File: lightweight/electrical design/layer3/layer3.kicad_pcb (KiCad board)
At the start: 2 copper layers, 188.9 x 115 mm, 59 parts, among them J1 SH1.0 5P, J11 SH1.0 5P, J2 SH1.0 5P, J3 SH1.0 5P, J4 SH1.0 5P, J5 Conn_01x03_Pin, J6 SH1.0 Female, SW1 SW_SPDT, SW2 SW_DPDT_x2, SW5 SW_Push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

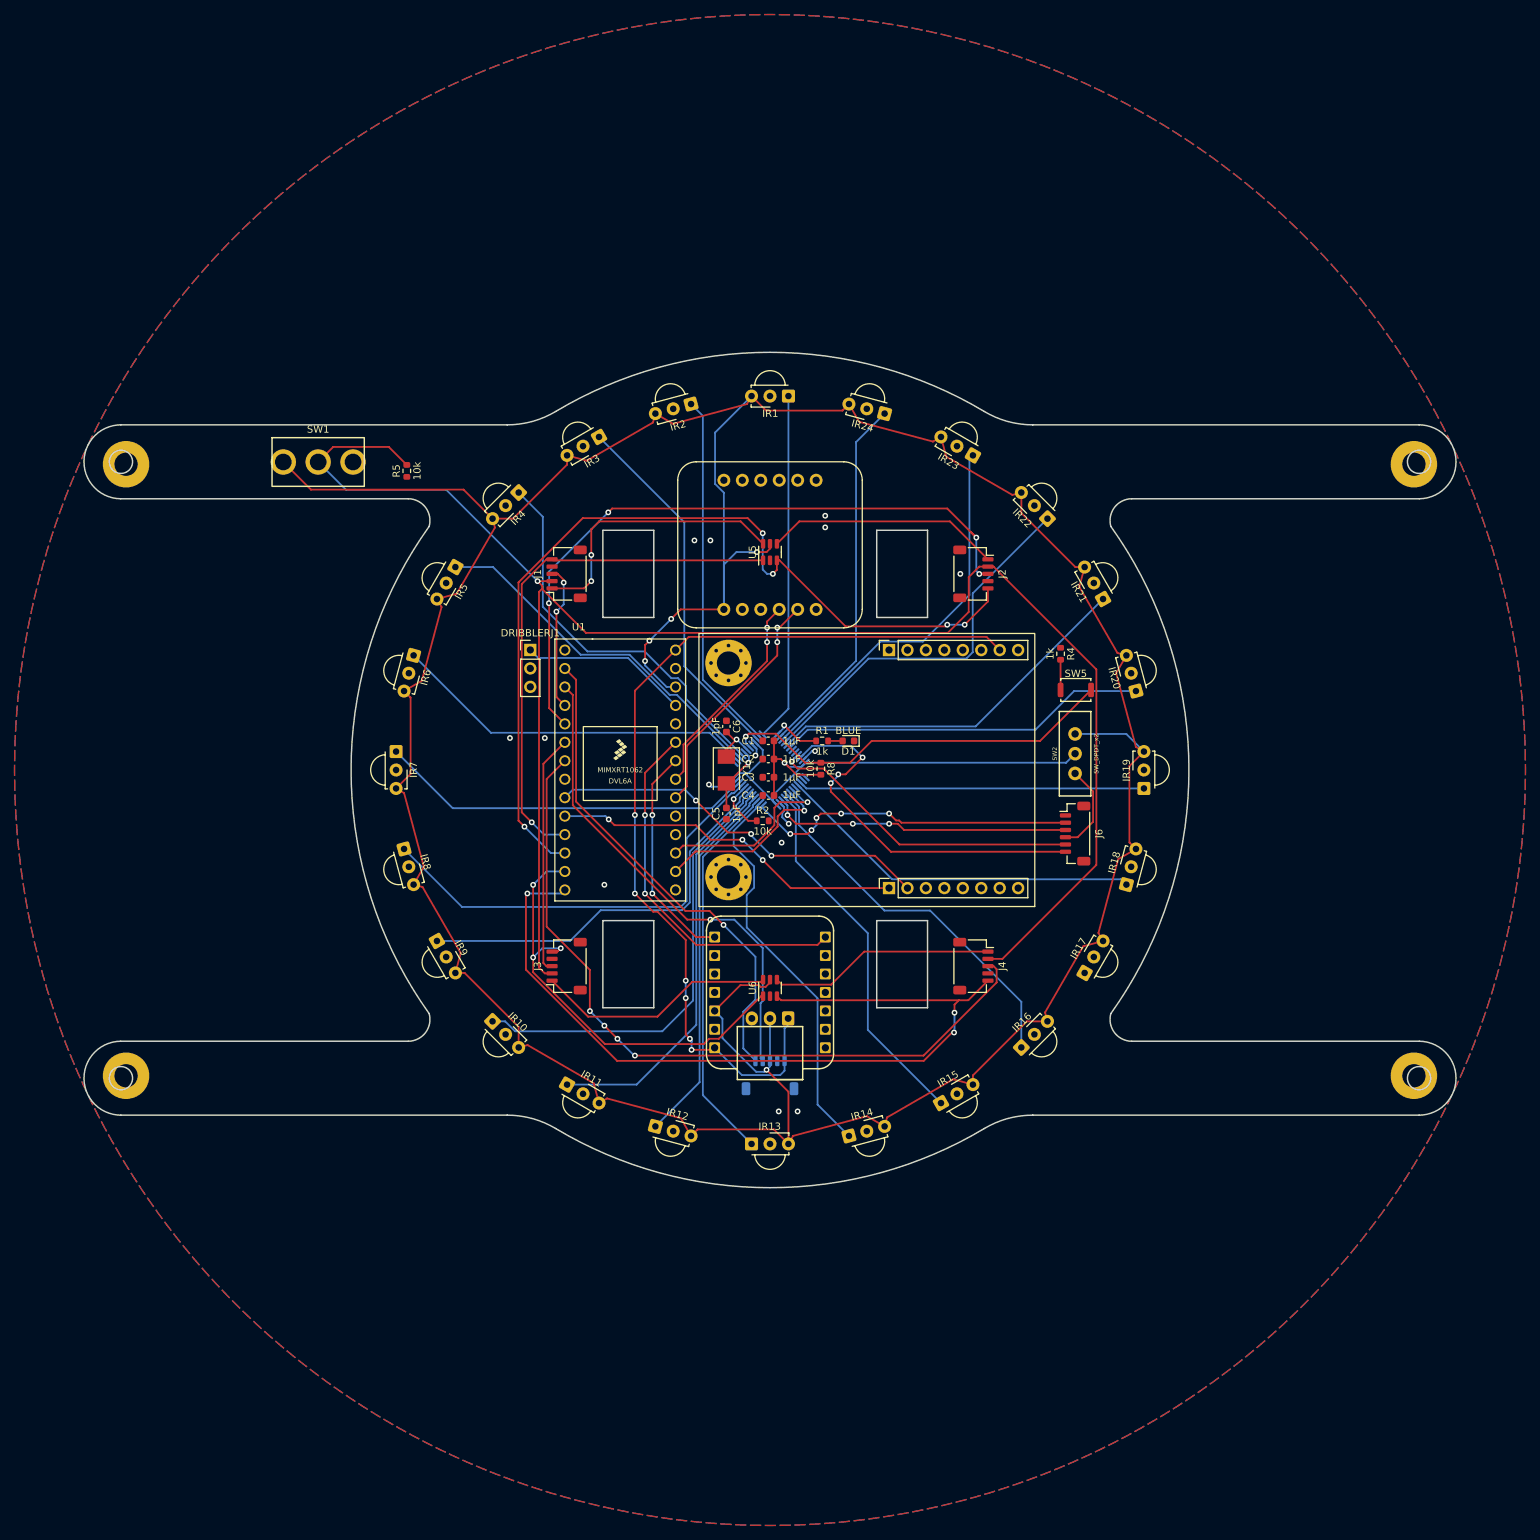
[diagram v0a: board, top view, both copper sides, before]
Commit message: fix drc faults on l1, l2, and l3 pcbs
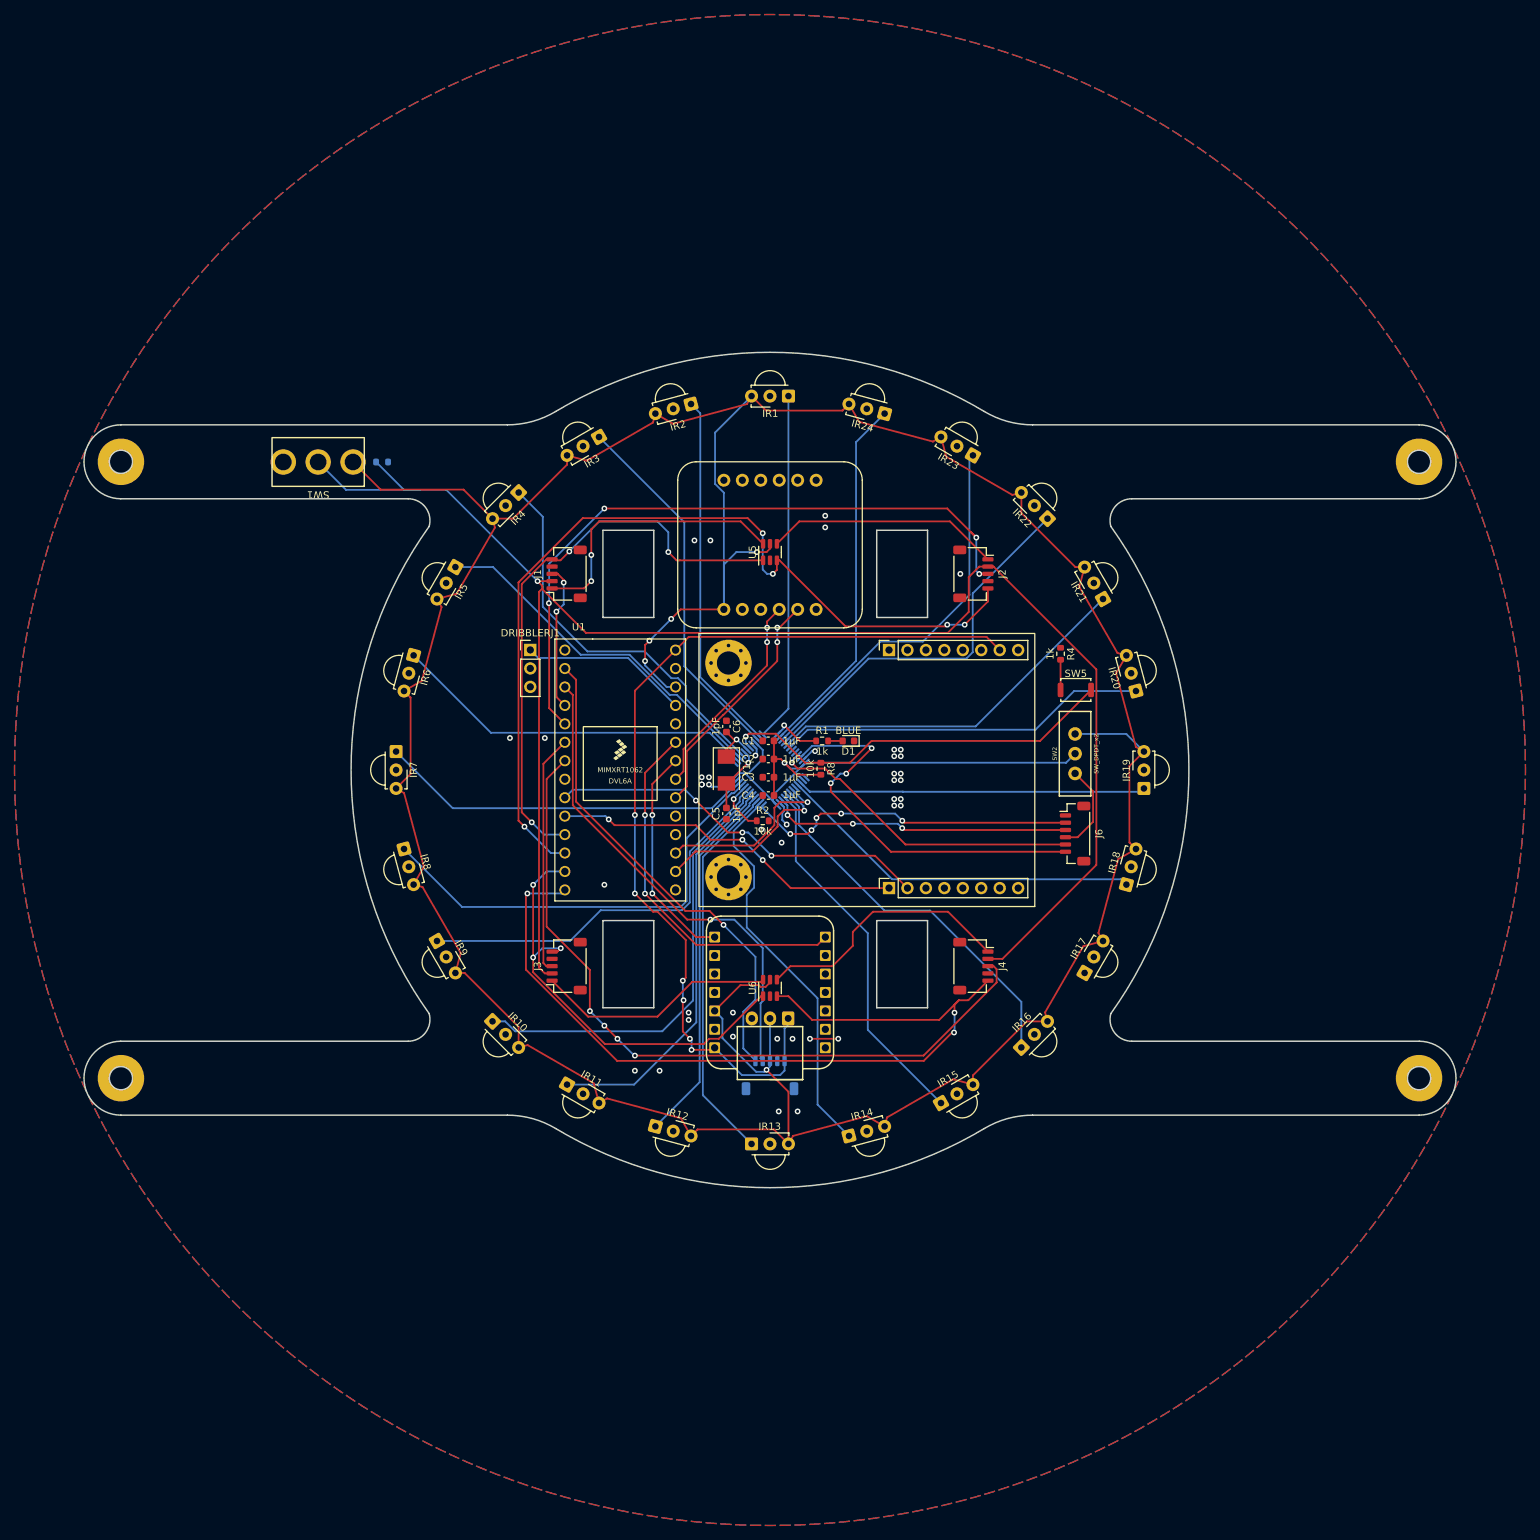
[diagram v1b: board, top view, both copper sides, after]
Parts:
- R5: moved to B.Cu
- moved R5 3.61 mm to (51.6, 62.6), turned to 180 degrees
- moved H1 0.78 mm to (15.6, 62.6)
- moved H3 0.78 mm to (15.6, 147.4)
- moved H2 0.78 mm to (194.4, 62.6)
- moved H4 0.78 mm to (194.4, 147.4)
- turned SW1 to 180 degrees
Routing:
- net +3V3: track 500.3 -> 490.7 mm
- net /EN: track 247.4 -> 240.9 mm
- net /M1INA: track 73.3 -> 79.4 mm, vias 1 -> 3
- net /M4INB: track 31.2 -> 36.3 mm
- net GND: track 11.9 -> 15.8 mm, vias 15 -> 42
- net /ir/DEBUGRX: track 52.7 -> 55.1 mm
- net /M4INA: track 116.9 -> 119.2 mm
- net /M2PWM: track 93.3 -> 94.0 mm

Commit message: add lw pcb files
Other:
- board text added: "JLCJLCJLCJLC"
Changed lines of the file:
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@@
       (disableapertmacros false)
       (usegerberextensions true)
-      (usegerberattributes true)
-      (usegerberadvancedattributes true)
+      (usegerberattributes false)
+      (usegerberadvancedattributes false)
       (creategerberjobfile false)
       (dashed_line_dash_ratio 12.000000)
@@
     (pad "5" smd roundrect (at 2 -2 90) (size 0.6 1.55) (layers "F.Cu" "F.Paste" "F.Mask") (roundrect_rratio 0.25)
       (net 9 "/M3INA") (pinfunction "Pin_5") (pintype "passive"))
-    (pad "MP" smd roundrect (at -3.3 1.875 90) (size 1.2 1.8) (layers "F.Cu" "F.Paste" "F.Mask") (roundrect_rratio 0.208333))
-    (pad "MP" smd roundrect (at 3.3 1.875 90) (size 1.2 1.8) (layers "F.Cu" "F.Paste" "F.Mask") (roundrect_rratio 0.208333))
+    (pad "MP" smd roundrect (at -3.3 1.875 90) (size 1.2 1.8) (layers "F.Cu" "F.Paste" "F.Mask") (roundrect_rratio 0.2083333333))
+    (pad "MP" smd roundrect (at 3.3 1.875 90) (size 1.2 1.8) (layers "F.Cu" "F.Paste" "F.Mask") (roundrect_rratio 0.2083333333))
     (model "${KICAD6_3DMODEL_DIR}/Connector_JST.3dshapes/JST_SH_SM05B-SRSS-TB_1x05-1MP_P1.00mm_Horizontal.step"
       (offset (xyz 0 1 0))
@@
     (pad "5" smd roundrect (at 2 -2 270) (size 0.6 1.55) (layers "F.Cu" "F.Paste" "F.Mask") (roundrect_rratio 0.25)
       (net 6 "/M2INA") (pinfunction "Pin_5") (pintype "passive"))
-    (pad "MP" smd roundrect (at -3.3 1.875 270) (size 1.2 1.8) (layers "F.Cu" "F.Paste" "F.Mask") (roundrect_rratio 0.208333))
-    (pad "MP" smd roundrect (at 3.3 1.875 270) (size 1.2 1.8) (layers "F.Cu" "F.Paste" "F.Mask") (roundrect_rratio 0.208333))
+    (pad "MP" smd roundrect (at -3.3 1.875 270) (size 1.2 1.8) (layers "F.Cu" "F.Paste" "F.Mask") (roundrect_rratio 0.2083333333))
+    (pad "MP" smd roundrect (at 3.3 1.875 270) (size 1.2 1.8) (layers "F.Cu" "F.Paste" "F.Mask") (roundrect_rratio 0.2083333333))
     (model "${KICAD6_3DMODEL_DIR}/Connector_JST.3dshapes/JST_SH_SM05B-SRSS-TB_1x05-1MP_P1.00mm_Horizontal.step"
       (offset (xyz 0 1 0))
@@
     (pad "5" smd roundrect (at 2 -2 90) (size 0.6 1.55) (layers "F.Cu" "F.Paste" "F.Mask") (roundrect_rratio 0.25)
       (net 3 "/M1INA") (pinfunction "Pin_5") (pintype "passive"))
-    (pad "MP" smd roundrect (at -3.3 1.875 90) (size 1.2 1.8) (layers "F.Cu" "F.Paste" "F.Mask") (roundrect_rratio 0.208333))
-    (pad "MP" smd roundrect (at 3.3 1.875 90) (size 1.2 1.8) (layers "F.Cu" "F.Paste" "F.Mask") (roundrect_rratio 0.208333))
+    (pad "MP" smd roundrect (at -3.3 1.875 90) (size 1.2 1.8) (layers "F.Cu" "F.Paste" "F.Mask") (roundrect_rratio 0.2083333333))
+    (pad "MP" smd roundrect (at 3.3 1.875 90) (size 1.2 1.8) (layers "F.Cu" "F.Paste" "F.Mask") (roundrect_rratio 0.2083333333))
     (model "${KICAD6_3DMODEL_DIR}/Connector_JST.3dshapes/JST_SH_SM05B-SRSS-TB_1x05-1MP_P1.00mm_Horizontal.step"
       (offset (xyz 0 1 0))
@@
     (pad "5" smd roundrect (at 2 -2 270) (size 0.6 1.55) (layers "F.Cu" "F.Paste" "F.Mask") (roundrect_rratio 0.25)
       (net 12 "/M4INA") (pinfunction "Pin_5") (pintype "passive"))
-    (pad "MP" smd roundrect (at -3.3 1.875 270) (size 1.2 1.8) (layers "F.Cu" "F.Paste" "F.Mask") (roundrect_rratio 0.208333))
-    (pad "MP" smd roundrect (at 3.3 1.875 270) (size 1.2 1.8) (layers "F.Cu" "F.Paste" "F.Mask") (roundrect_rratio 0.208333))
+    (pad "MP" smd roundrect (at -3.3 1.875 270) (size 1.2 1.8) (layers "F.Cu" "F.Paste" "F.Mask") (roundrect_rratio 0.2083333333))
+    (pad "MP" smd roundrect (at 3.3 1.875 270) (size 1.2 1.8) (layers "F.Cu" "F.Paste" "F.Mask") (roundrect_rratio 0.2083333333))
     (model "${KICAD6_3DMODEL_DIR}/Connector_JST.3dshapes/JST_SH_SM05B-SRSS-TB_1x05-1MP_P1.00mm_Horizontal.step"
       (offset (xyz 0 1 0))
@@
     (pad "6" smd roundrect (at 2.5 1.325 270) (size 0.6 1.55) (layers "F.Cu" "F.Paste" "F.Mask") (roundrect_rratio 0.25)
       (net 49 "/ir/DEBUGRX") (pinfunction "Pin_6") (pintype "passive"))
-    (pad "MP" smd roundrect (at -3.8 -1.2 270) (size 1.2 1.8) (layers "F.Cu" "F.Paste" "F.Mask") (roundrect_rratio 0.208333))
-    (pad "MP" smd roundrect (at 3.8 -1.2 270) (size 1.2 1.8) (layers "F.Cu" "F.Paste" "F.Mask") (roundrect_rratio 0.208333))
+    (pad "MP" smd roundrect (at -3.8 -1.2 270) (size 1.2 1.8) (layers "F.Cu" "F.Paste" "F.Mask") (roundrect_rratio 0.2083333333))
+    (pad "MP" smd roundrect (at 3.8 -1.2 270) (size 1.2 1.8) (layers "F.Cu" "F.Paste" "F.Mask") (roundrect_rratio 0.2083333333))
     (model "${KICAD6_3DMODEL_DIR}/Connector_JST.3dshapes/JST_SH_BM06B-SRSS-TB_1x06-1MP_P1.00mm_Vertical.step"
       (offset (xyz 0 1 0))
@@
     (pad "5" smd roundrect (at 2 2 180) (size 0.6 1.55) (layers "B.Cu" "B.Paste" "B.Mask") (roundrect_rratio 0.25)
       (net 18 "/L1TX") (pinfunction "Pin_5") (pintype "passive"))
-    (pad "MP" smd roundrect (at -3.3 -1.875 180) (size 1.2 1.8) (layers "B.Cu" "B.Paste" "B.Mask") (roundrect_rratio 0.208333))
-    (pad "MP" smd roundrect (at 3.3 -1.875 180) (size 1.2 1.8) (layers "B.Cu" "B.Paste" "B.Mask") (roundrect_rratio 0.208333))
+    (pad "MP" smd roundrect (at -3.3 -1.875 180) (size 1.2 1.8) (layers "B.Cu" "B.Paste" "B.Mask") (roundrect_rratio 0.2083333333))
+    (pad "MP" smd roundrect (at 3.3 -1.875 180) (size 1.2 1.8) (layers "B.Cu" "B.Paste" "B.Mask") (roundrect_rratio 0.2083333333))
     (model "${KICAD6_3DMODEL_DIR}/Connector_JST.3dshapes/JST_SH_SM05B-SRSS-TB_1x05-1MP_P1.00mm_Horizontal.step"
       (offset (xyz 0 1 0))
@@
     (fp_line (start 7.45 2.35) (end -2.45 2.35)
       (stroke (width 0.1) (type solid)) (layer "B.Fab"))
-    (pad "1" thru_hole roundrect (at 0 0 180) (size 1.7 1.95) (drill 0.95) (layers "*.Cu" "*.Mask") (roundrect_rratio 0.147059)
+    (pad "1" thru_hole roundrect (at 0 0 180) (size 1.7 1.95) (drill 0.95) (layers "*.Cu" "*.Mask") (roundrect_rratio 0.1470588235)
       (net 13 "+5V") (pinfunction "Pin_1") (pintype "passive"))
     (pad "2" thru_hole oval (at 2.5 0 180) (size 1.7 1.95) (drill 0.95) (layers "*.Cu" "*.Mask")
@@
   (gr_arc (start 75.500365 55.643931) (mid 72.290367 57.016406) (end 68.830882 57.485168)
     (stroke (width 0.2) (type solid)) (layer "Edge.Cuts"))
+  (gr_text "JLCJLCJLCJLC" (at 105 80.2) (layer "F.SilkS")
+    (effects (font (size 1 1) (thickness 0.2) bold))
+  )
   (segment (start 81.492588 70.775) (end 80.4 71.867588) (width 0.25) (layer "F.Cu") (net 1))
   (segment (start 79.4 80) (end 75 80) (width 0.25) (layer "F.Cu") (net 1))

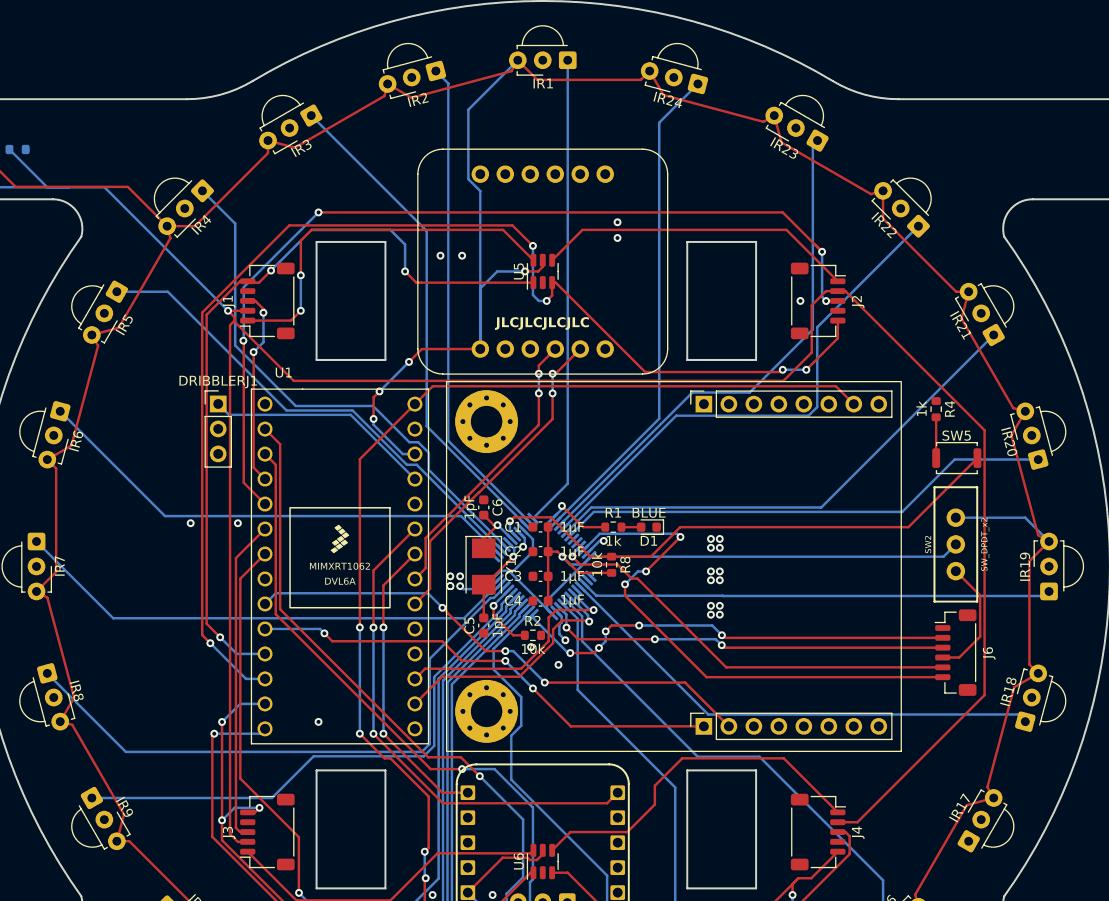
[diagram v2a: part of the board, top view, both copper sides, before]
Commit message: rerouted lw l3 ir stm circuit
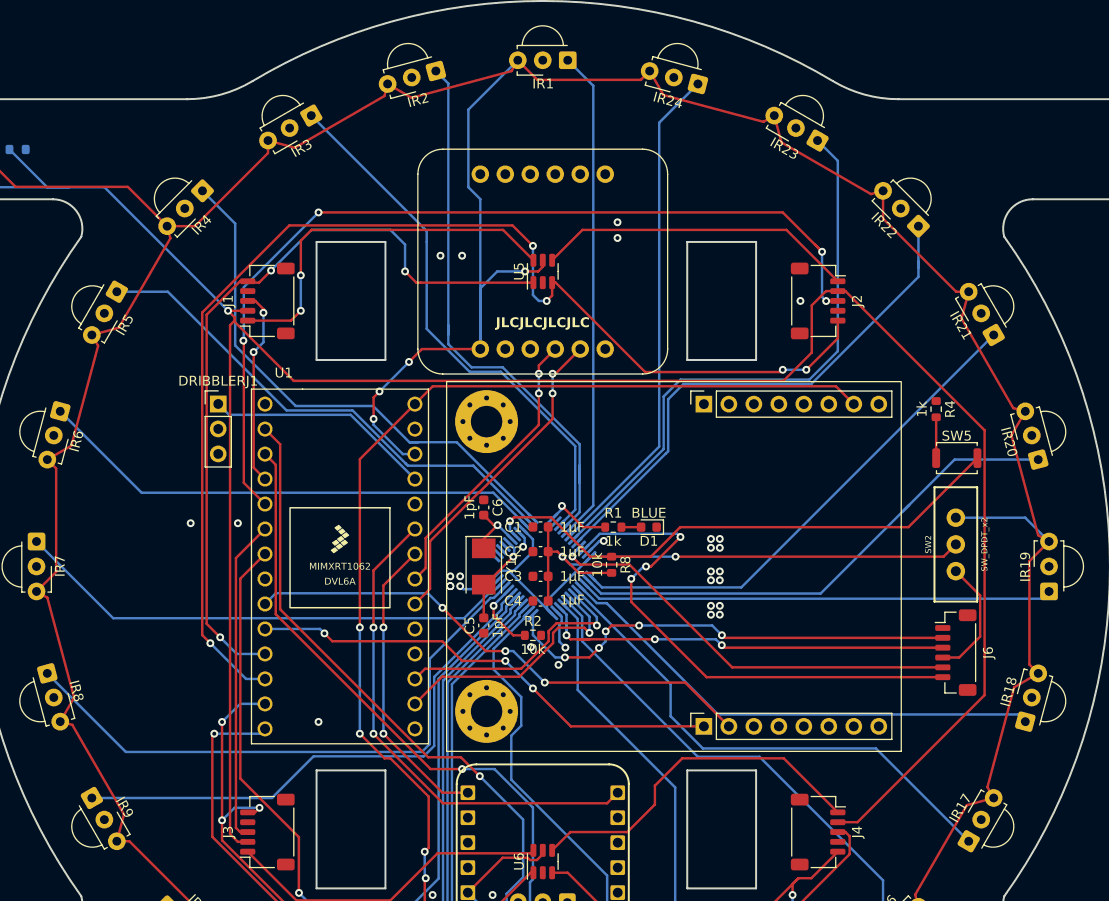
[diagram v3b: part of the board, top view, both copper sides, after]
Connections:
- U7 pad 10: /ir/IR3 -> /ir/IR6
- U7 pad 11: /ir/IR2 -> /ir/IR5
- U7 pad 12: /ir/IR1 -> /ir/IR4
- U7 pad 14: /ir/IR24 -> unconnected-(U7-PA4-Pad14)
- U7 pad 15: /ir/IR23 -> /ir/IR3
- U7 pad 16: /ir/IR22 -> /ir/IR2
- U7 pad 17: /ir/IR21 -> /ir/IR1
- U7 pad 18: /ir/IR20 -> /ir/IR24
- U7 pad 19: unconnected-(U7-PB1-Pad19) -> /ir/IR23
- U7 pad 2: /ir/IR6 -> unconnected-(U7-PC13-Pad2)
- U7 pad 20: unconnected-(U7-PB2-Pad20) -> /ir/IR22
- U7 pad 25: unconnected-(U7-PB12-Pad25) -> /ir/IR21
- U7 pad 26: unconnected-(U7-PB13-Pad26) -> /ir/IR20
- U7 pad 29: unconnected-(U7-PA8-Pad29) -> /ir/IR17
- U7 pad 3: /ir/IR5 -> unconnected-(U7-PC14-Pad3)
- U7 pad 4: /ir/IR4 -> unconnected-(U7-PC15-Pad4)
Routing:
- net /ir/IR17: track 0.00 -> 52.3 mm
- net /ir/IR2: track 49.8 -> 58.7 mm
- net /ir/IR23: track 53.4 -> 60.2 mm
- net /ir/IR3: track 50.7 -> 55.3 mm
- net /ir/SWDIO: track 41.4 -> 44.4 mm
- net /ir/IR20: track 50.8 -> 53.1 mm
- net /ir/IR1: track 48.1 -> 50.2 mm
- net /ir/IR5: track 50.0 -> 51.9 mm
- net /ir/IR6: track 50.5 -> 52.2 mm
- net /ir/IR4: track 54.0 -> 55.5 mm
- net /ir/SWDCLOCK: track 45.8 -> 47.2 mm
- net /ir/IR22: track 53.6 -> 54.9 mm
- net IRRX: track 25.5 -> 26.4 mm
- net /ir/IR24: track 50.5 -> 51.3 mm
- net GND: track 15.8 -> 16.5 mm
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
